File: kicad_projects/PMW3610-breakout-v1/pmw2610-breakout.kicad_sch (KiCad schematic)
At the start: 17 parts, among them J1 Conn_01x06_Pin, J3 Conn_01x01_Pin, J4 Conn_01x01_Pin, J5 Conn_01x01_Pin, J6 Conn_01x01_Pin, J7 Conn_01x01_Pin, U1 PMW3610, U2 TLV70018_SOT23-5

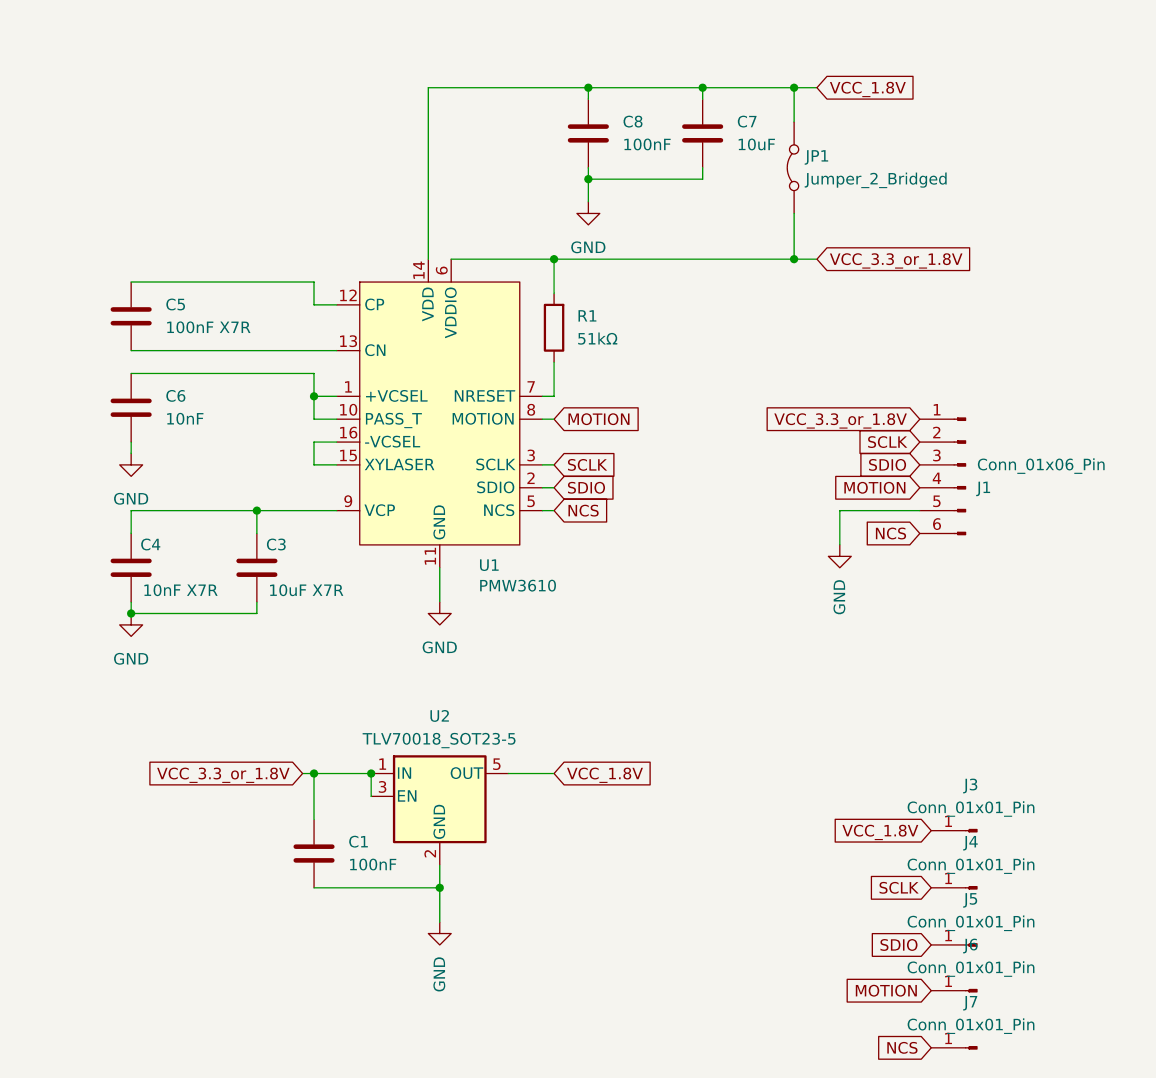
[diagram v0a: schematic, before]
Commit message: Remove GPS info from pictures and re-commit :( * Add readme * Add PMW3610-breakout-v1 old version PCB * Add Readme and pictures. Rename PMW3610-breakout to PMW3610-breakout-v2
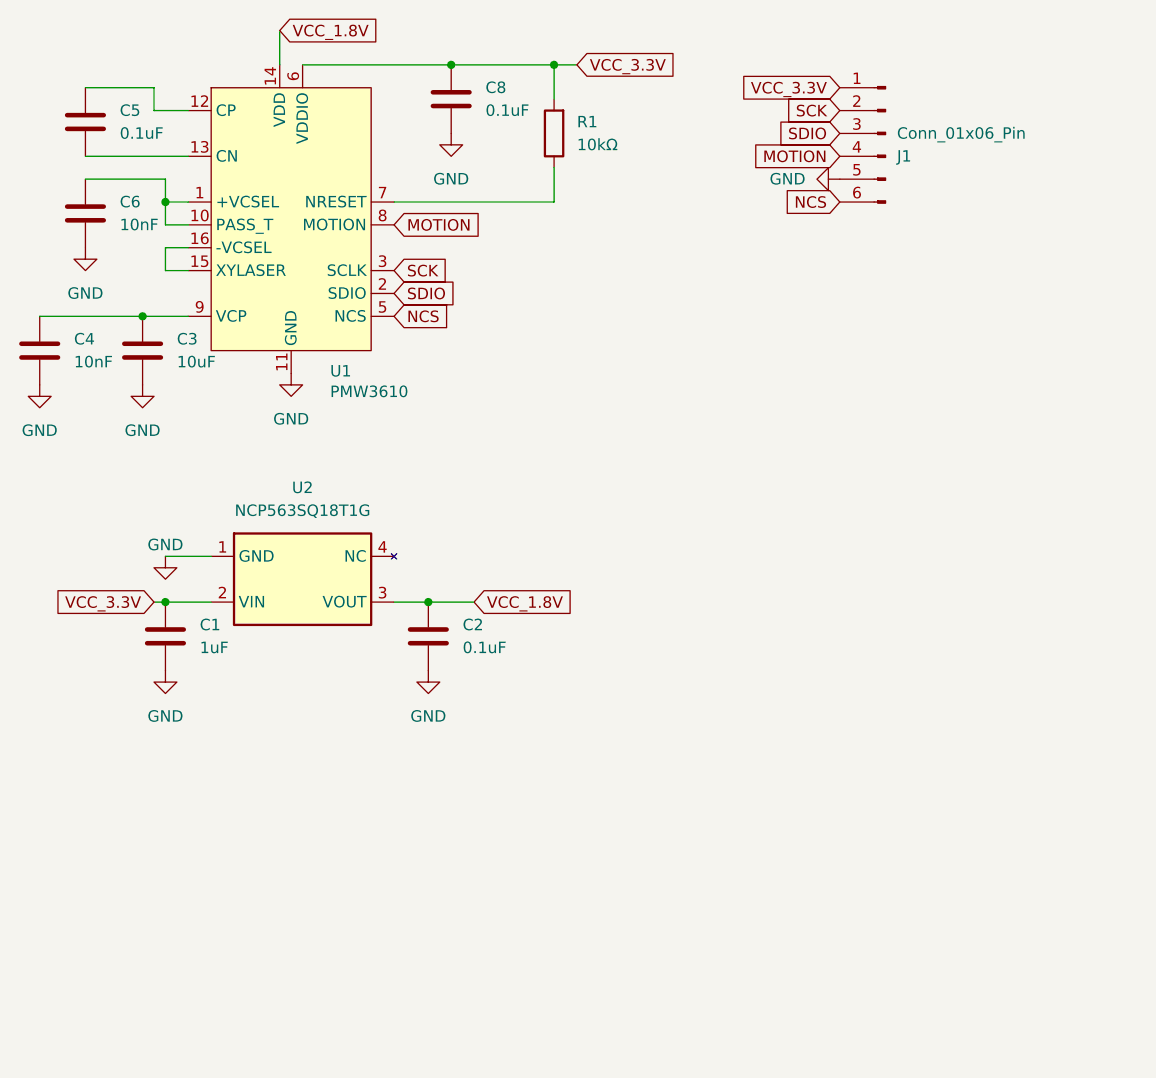
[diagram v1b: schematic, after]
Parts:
- removed C7: 10uF, Capacitor_SMD:C_0603_1608Metric, symbol Device:C
- removed J3, J4, J5, J6, J7: Conn_01x01_Pin, TestPoint:TestPoint_Pad_D1.0mm, symbol Connector:Conn_01x01_Pin
- removed JP1: Jumper_2_Bridged, Jumper:SolderJumper-2_P1.3mm_Bridged2Bar_RoundedPad1.0x1.5mm, symbol Jumper:Jumper_2_Bridged
- removed U2: TLV70018_SOT23-5, Package_TO_SOT_SMD:SOT-23-5, symbol Regulator_Linear:TLV70018_SOT23-5
- added C2: 0.1uF, Capacitor_SMD:C_0805_2012Metric, symbol Device:C
- added U2: NCP563SQ18T1G, Package_TO_SOT_SMD:SOT-343_SC-70-4, symbol 0_pmw3610-breakout:NCP563SQ18T1G
- C1: value 100nF -> 1uF; footprint Capacitor_SMD:C_0603_1608Metric -> Capacitor_SMD:C_0805_2012Metric; LCSC C14663 -> (none)
- C3: value 10uF X7R -> 10uF; footprint Capacitor_SMD:C_0603_1608Metric -> Capacitor_SMD:C_0805_2012Metric; LCSC C19702 -> (none)
- C4: value 10nF X7R -> 10nF; footprint Capacitor_SMD:C_0603_1608Metric -> Capacitor_SMD:C_0805_2012Metric; LCSC C57112 -> (none)
- C5: value 100nF X7R -> 0.1uF; footprint Capacitor_SMD:C_0603_1608Metric -> Capacitor_SMD:C_0805_2012Metric; LCSC C14663 -> (none)
- C6: footprint Capacitor_SMD:C_0603_1608Metric -> Capacitor_SMD:C_0805_2012Metric; LCSC C57112 -> (none)
- C8: value 100nF -> 0.1uF; footprint Capacitor_SMD:C_0603_1608Metric -> Capacitor_SMD:C_0805_2012Metric; LCSC C14663 -> (none)
- J1: footprint 0_pmw3610-breakout:JUSHUO-AFH34-S06FIA-1H -> Connector_FFC-FPC:TE_0-1734839-6_1x06-1MP_P0.5mm_Horizontal; LCSC C5139821 -> (none)
- R1: value 51kΩ -> 10kΩ; footprint Resistor_SMD:R_0603_1608Metric -> Resistor_SMD:R_0805_2012Metric; LCSC C23196 -> (none)
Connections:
- net GND: now also C2.2, U2.1 (GND)
- net VCC_1.8V: now also C2.1, U2.3 (VOUT); no longer C8.1
- net SCLK renamed SCK
- net VCC_3.3_or_1.8V renamed VCC_3.3V
- net VCC_3.3V: now also C8.1, U2.2 (VIN)
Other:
- moved on the sheet: C3, C4, C5, C6, C8, J1, R1, U1
